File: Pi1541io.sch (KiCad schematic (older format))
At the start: 50 parts, among them J1 IEC1, J10 SDA, J11 SCL, J12 I2C, J2 IEC2, J3 IEC3, J4 ExtSpkr, J5 GS3, J6 GS3, J7 GS3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

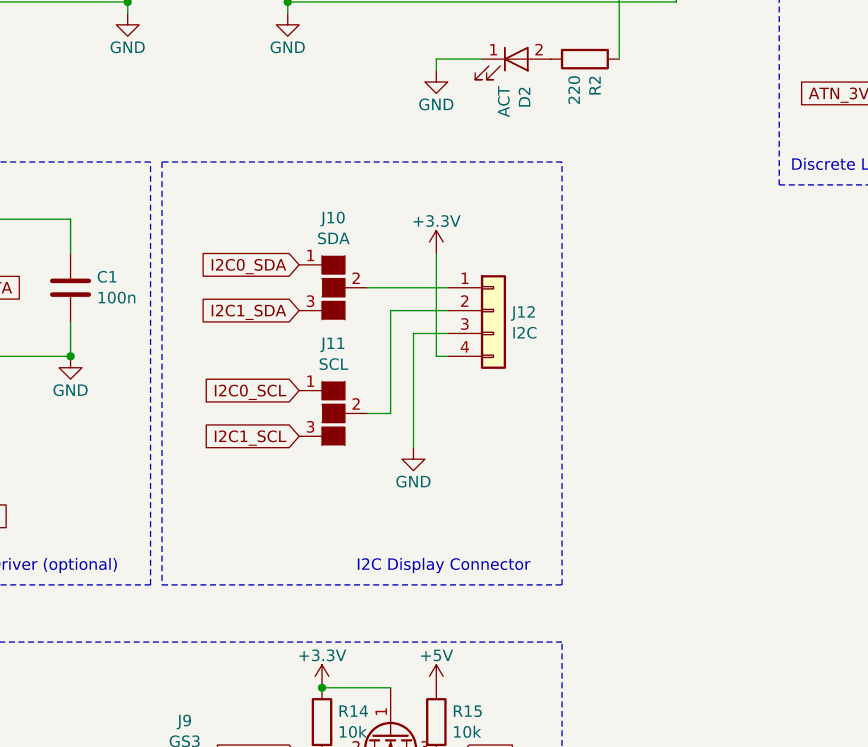
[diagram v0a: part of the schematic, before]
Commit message: I2C power pins now configurable.
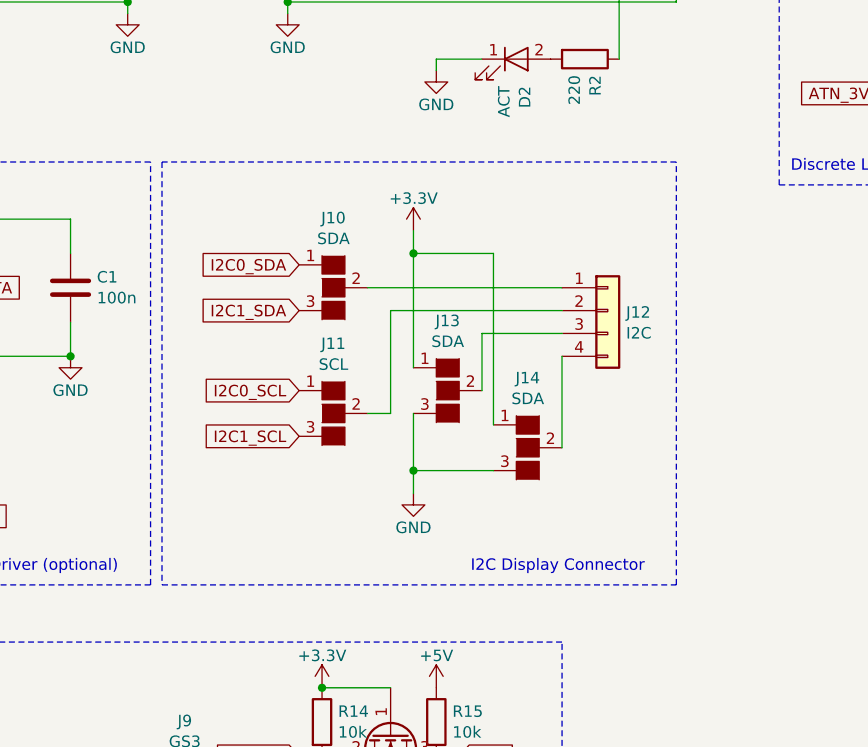
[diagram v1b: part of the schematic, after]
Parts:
- added J13, J14: SDA, Connectors:GS3, symbol conn:GS3
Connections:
- net +3V3: now also J13.1 (G1), J14.1 (G1); no longer J12.4 (Pin_4)
- net GND: now also J13.3 (G3), J14.3 (G3); no longer J12.3 (Pin_3)
- new net: J12.3 (Pin_3), J13.2 (G2)
- new net: J12.4 (Pin_4), J14.2 (G2)
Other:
- moved on the sheet: J12
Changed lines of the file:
@@
 L Pi1541io:Conn_01x04-Connector J12
 U 1 1 5B16BA02
-P 5000 4500
-F 0 "J12" H 5080 4492 50  0000 L CNN
-F 1 "I2C" H 5080 4401 50  0000 L CNN
-F 2 "Socket_Strips:Socket_Strip_Straight_1x04_Pitch2.54mm" H 5000 4500 50  0001 C CNN
-F 3 "~" H 5000 4500 50  0001 C CNN
-	1    5000 4500
+P 5500 4500
+F 0 "J12" H 5580 4492 50  0000 L CNN
+F 1 "I2C" H 5580 4401 50  0000 L CNN
+F 2 "Socket_Strips:Socket_Strip_Straight_1x04_Pitch2.54mm" H 5500 4500 50  0001 C CNN
+F 3 "~" H 5500 4500 50  0001 C CNN
+	1    5500 4500
 	1    0    0    -1
 $EndComp
@@
 $EndComp
 Wire Wire Line
-	4800 4400 4450 4400
-Wire Wire Line
-	4800 4600 4650 4600
-Wire Wire Line
-	4650 4600 4650 5100
-Wire Wire Line
-	4800 4700 4750 4700
-Wire Wire Line
-	4750 4700 4750 4250
+	5300 4400 4450 4400
 $Comp
 L power:GND #PWR0125
 U 1 1 5B1E56FA
-P 4650 5100
-F 0 "#PWR0125" H 4650 4850 50  0001 C CNN
-F 1 "GND" H 4650 4950 50  0000 C CNN
-F 2 "" H 4650 5100 50  0000 C CNN
-F 3 "" H 4650 5100 50  0000 C CNN
-	1    4650 5100
+P 4650 5300
+F 0 "#PWR0125" H 4650 5050 50  0001 C CNN
+F 1 "GND" H 4650 5150 50  0000 C CNN
+F 2 "" H 4650 5300 50  0000 C CNN
+F 3 "" H 4650 5300 50  0000 C CNN
+	1    4650 5300
 	1    0    0    -1
 $EndComp
 Wire Wire Line
-	4800 4500 4550 4500
+	5300 4500 4550 4500
 Wire Wire Line
 	4550 4500 4550 4950
@@
 	3550 3850 3550 5700
 Wire Notes Line
-	3550 5700 5300 5700
+	3550 5700 5800 5700
 Wire Notes Line
-	5300 5700 5300 3850
+	5800 5700 5800 3850
 Wire Notes Line
-	5300 3850 3550 3850
-Text Notes 4400 5650 0    50   ~ 0
+	5800 3850 3550 3850
+Text Notes 4900 5650 0    50   ~ 0
 I2C Display Connector
 $Comp
-L power:+3.3V #PWR?
+L power:+3.3V #PWR0124
 U 1 1 5B3C1A0C
-P 4750 4250
-F 0 "#PWR?" H 4750 4100 50  0001 C CNN
-F 1 "+3.3V" H 4750 4390 50  0000 C CNN
-F 2 "" H 4750 4250 50  0000 C CNN
-F 3 "" H 4750 4250 50  0000 C CNN
-	1    4750 4250
+P 4650 4150
+F 0 "#PWR0124" H 4650 4000 50  0001 C CNN
+F 1 "+3.3V" H 4650 4290 50  0000 C CNN
+F 2 "" H 4650 4150 50  0000 C CNN
+F 3 "" H 4650 4150 50  0000 C CNN
+	1    4650 4150
 	1    0    0    -1
 $EndComp
+$Comp
+L conn:GS3 J13
+U 1 1 5B409F64
+P 4800 4850
+F 0 "J13" H 4800 5155 50  0000 C CNN
+F 1 "SDA" H 4800 5064 50  0000 C CNN
+F 2 "Connectors:GS3" V 4888 4776 50  0001 C CNN
+F 3 "" H 4800 4850 50  0001 C CNN
+	1    4800 4850
+	1    0    0    -1
+$EndComp
+$Comp
+L conn:GS3 J14
+U 1 1 5B413348
+P 5150 5100
+F 0 "J14" H 5150 5405 50  0000 C CNN
+F 1 "SDA" H 5150 5314 50  0000 C CNN
+F 2 "Connectors:GS3" V 5238 5026 50  0001 C CNN
+F 3 "" H 5150 5100 50  0001 C CNN
+	1    5150 5100
+	1    0    0    -1
+$EndComp
+Wire Wire Line
+	5300 5100 5300 4700
+Wire Wire Line
+	5300 4600 4950 4600
+Wire Wire Line
+	4950 4600 4950 4850
+Wire Wire Line
+	4650 4950 4650 5200
+Wire Wire Line
+	5000 5200 4650 5200
+Connection ~ 4650 5200
+Wire Wire Line
+	4650 5200 4650 5300
+Wire Wire Line
+	4650 4750 4650 4250
+Wire Wire Line
+	5000 5000 5000 4250
+Wire Wire Line
+	5000 4250 4650 4250
+Connection ~ 4650 4250
+Wire Wire Line
+	4650 4250 4650 4150
 $EndSCHEMATC

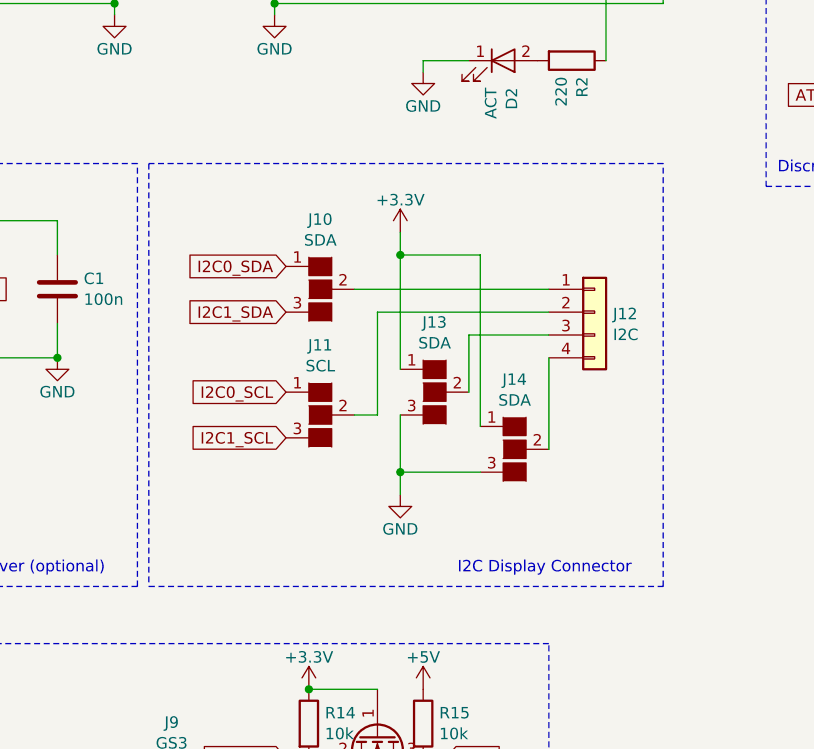
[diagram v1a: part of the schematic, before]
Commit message: Both voltage and pin order now configurable.
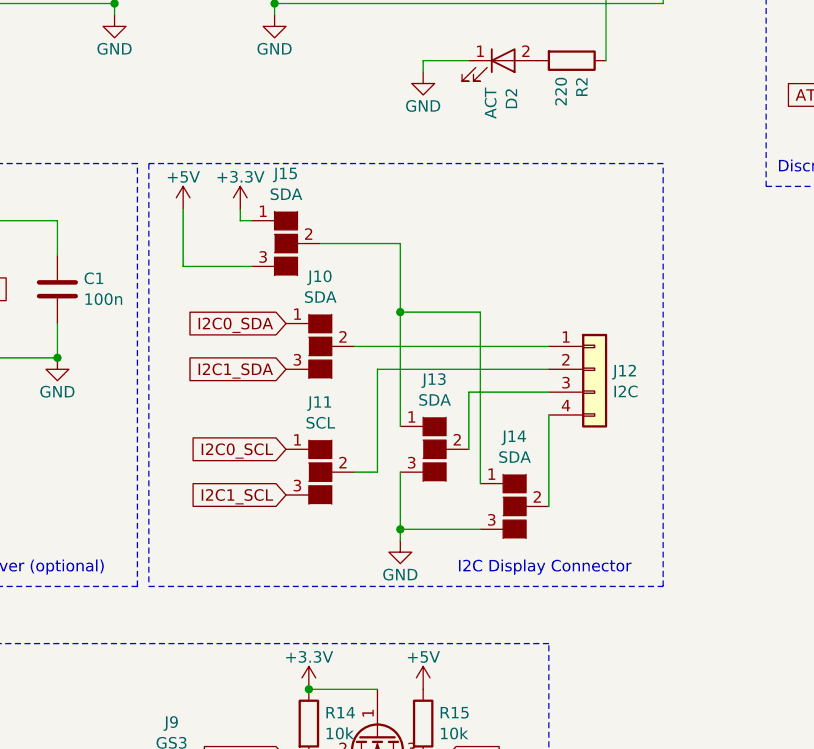
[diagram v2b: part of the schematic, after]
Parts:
- added J15: SDA, Connectors:GS3, symbol conn:GS3
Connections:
- net +3V3: now also J15.1 (G1); no longer J13.1 (G1), J14.1 (G1)
- net +5V: now also J15.3 (G3)
- new net: J13.1 (G1), J14.1 (G1), J15.2 (G2)
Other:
- moved on the sheet: J10, J11, J12, J13, J14
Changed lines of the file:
@@
 Sheet 1 1
 Title "Pi1541 IO Adapter"
-Date "2018-07-05"
+Date "2018-07-08"
 Rev "4"
 Comp "hackup.net"
@@
 L Pi1541io:Conn_01x04-Connector J12
 U 1 1 5B16BA02
-P 5500 4500
-F 0 "J12" H 5580 4492 50  0000 L CNN
-F 1 "I2C" H 5580 4401 50  0000 L CNN
-F 2 "Socket_Strips:Socket_Strip_Straight_1x04_Pitch2.54mm" H 5500 4500 50  0001 C CNN
-F 3 "~" H 5500 4500 50  0001 C CNN
-	1    5500 4500
+P 5500 4750
+F 0 "J12" H 5580 4742 50  0000 L CNN
+F 1 "I2C" H 5580 4651 50  0000 L CNN
+F 2 "Socket_Strips:Socket_Strip_Straight_1x04_Pitch2.54mm" H 5500 4750 50  0001 C CNN
+F 3 "~" H 5500 4750 50  0001 C CNN
+	1    5500 4750
 	1    0    0    -1
 $EndComp
@@
 L conn:GS3 J10
 U 1 1 5B1BB247
-P 4300 4400
-F 0 "J10" H 4300 4705 50  0000 C CNN
-F 1 "SDA" H 4300 4614 50  0000 C CNN
-F 2 "Connectors:GS3" V 4388 4326 50  0001 C CNN
-F 3 "" H 4300 4400 50  0001 C CNN
-	1    4300 4400
+P 4300 4650
+F 0 "J10" H 4300 4955 50  0000 C CNN
+F 1 "SDA" H 4300 4864 50  0000 C CNN
+F 2 "Connectors:GS3" V 4388 4576 50  0001 C CNN
+F 3 "" H 4300 4650 50  0001 C CNN
+	1    4300 4650
 	1    0    0    -1
 $EndComp
@@
 L conn:GS3 J11
 U 1 1 5B1BB619
-P 4300 4950
-F 0 "J11" H 4300 5255 50  0000 C CNN
-F 1 "SCL" H 4300 5164 50  0000 C CNN
-F 2 "Connectors:GS3" V 4388 4876 50  0001 C CNN
-F 3 "" H 4300 4950 50  0001 C CNN
-	1    4300 4950
-	1    0    0    -1
-$EndComp
-Wire Wire Line
-	5300 4400 4450 4400
+P 4300 5200
+F 0 "J11" H 4300 5505 50  0000 C CNN
+F 1 "SCL" H 4300 5414 50  0000 C CNN
+F 2 "Connectors:GS3" V 4388 5126 50  0001 C CNN
+F 3 "" H 4300 5200 50  0001 C CNN
+	1    4300 5200
+	1    0    0    -1
+$EndComp
+Wire Wire Line
+	5300 4650 4450 4650
 $Comp
 L power:GND #PWR0125
 U 1 1 5B1E56FA
-P 4650 5300
-F 0 "#PWR0125" H 4650 5050 50  0001 C CNN
-F 1 "GND" H 4650 5150 50  0000 C CNN
-F 2 "" H 4650 5300 50  0000 C CNN
-F 3 "" H 4650 5300 50  0000 C CNN
-	1    4650 5300
-	1    0    0    -1
-$EndComp
-Wire Wire Line
-	5300 4500 4550 4500
-Wire Wire Line
-	4550 4500 4550 4950
-Wire Wire Line
-	4550 4950 4450 4950
-Text GLabel 4150 4300 0    50   Input ~ 0
+P 4650 5500
+F 0 "#PWR0125" H 4650 5250 50  0001 C CNN
+F 1 "GND" H 4650 5350 50  0000 C CNN
+F 2 "" H 4650 5500 50  0000 C CNN
+F 3 "" H 4650 5500 50  0000 C CNN
+	1    4650 5500
+	1    0    0    -1
+$EndComp
+Wire Wire Line
+	5300 4750 4550 4750
+Wire Wire Line
+	4550 4750 4550 5200
+Wire Wire Line
+	4550 5200 4450 5200
+Text GLabel 4150 4550 0    50   Input ~ 0
 I2C0_SDA
-Text GLabel 4150 4500 0    50   Input ~ 0
+Text GLabel 4150 4750 0    50   Input ~ 0
 I2C1_SDA
-Text GLabel 4150 4850 0    50   Input ~ 0
+Text GLabel 4150 5100 0    50   Input ~ 0
 I2C0_SCL
-Text GLabel 4150 5050 0    50   Input ~ 0
+Text GLabel 4150 5300 0    50   Input ~ 0
 I2C1_SCL
 Wire Wire Line
@@
 L power:+3.3V #PWR0124
 U 1 1 5B3C1A0C
-P 4650 4150
-F 0 "#PWR0124" H 4650 4000 50  0001 C CNN
-F 1 "+3.3V" H 4650 4290 50  0000 C CNN
-F 2 "" H 4650 4150 50  0000 C CNN
-F 3 "" H 4650 4150 50  0000 C CNN
-	1    4650 4150
+P 3950 4050
+F 0 "#PWR0124" H 3950 3900 50  0001 C CNN
+F 1 "+3.3V" H 3950 4190 50  0000 C CNN
+F 2 "" H 3950 4050 50  0000 C CNN
+F 3 "" H 3950 4050 50  0000 C CNN
+	1    3950 4050
 	1    0    0    -1
 $EndComp
@@
 L conn:GS3 J13
 U 1 1 5B409F64
-P 4800 4850
-F 0 "J13" H 4800 5155 50  0000 C CNN
-F 1 "SDA" H 4800 5064 50  0000 C CNN
-F 2 "Connectors:GS3" V 4888 4776 50  0001 C CNN
-F 3 "" H 4800 4850 50  0001 C CNN
-	1    4800 4850
+P 4800 5100
+F 0 "J13" H 4800 5405 50  0000 C CNN
+F 1 "SDA" H 4800 5314 50  0000 C CNN
+F 2 "Connectors:GS3" V 4888 5026 50  0001 C CNN
+F 3 "" H 4800 5100 50  0001 C CNN
+	1    4800 5100
 	1    0    0    -1
 $EndComp
@@
 L conn:GS3 J14
 U 1 1 5B413348
-P 5150 5100
-F 0 "J14" H 5150 5405 50  0000 C CNN
-F 1 "SDA" H 5150 5314 50  0000 C CNN
-F 2 "Connectors:GS3" V 5238 5026 50  0001 C CNN
-F 3 "" H 5150 5100 50  0001 C CNN
-	1    5150 5100
-	1    0    0    -1
-$EndComp
-Wire Wire Line
-	5300 5100 5300 4700
-Wire Wire Line
-	5300 4600 4950 4600
-Wire Wire Line
-	4950 4600 4950 4850
-Wire Wire Line
-	4650 4950 4650 5200
-Wire Wire Line
-	5000 5200 4650 5200
-Connection ~ 4650 5200
-Wire Wire Line
-	4650 5200 4650 5300
-Wire Wire Line
-	4650 4750 4650 4250
-Wire Wire Line
-	5000 5000 5000 4250
-Wire Wire Line
-	5000 4250 4650 4250
-Connection ~ 4650 4250
-Wire Wire Line
-	4650 4250 4650 4150
+P 5150 5350
+F 0 "J14" H 5150 5655 50  0000 C CNN
+F 1 "SDA" H 5150 5564 50  0000 C CNN
+F 2 "Connectors:GS3" V 5238 5276 50  0001 C CNN
+F 3 "" H 5150 5350 50  0001 C CNN
+	1    5150 5350
+	1    0    0    -1
+$EndComp
+Wire Wire Line
+	5300 5350 5300 4950
+Wire Wire Line
+	5300 4850 4950 4850
+Wire Wire Line
+	4950 4850 4950 5100
+Wire Wire Line
+	4650 5200 4650 5450
+Wire Wire Line
+	5000 5450 4650 5450
+Connection ~ 4650 5450
+Wire Wire Line
+	4650 5450 4650 5500
+Wire Wire Line
+	4650 5000 4650 4500
+Wire Wire Line
+	5000 5250 5000 4500
+Wire Wire Line
+	5000 4500 4650 4500
+Connection ~ 4650 4500
+$Comp
+L conn:GS3 J15
+U 1 1 5B44E5B6
+P 4150 4200
+F 0 "J15" H 4150 4505 50  0000 C CNN
+F 1 "SDA" H 4150 4414 50  0000 C CNN
+F 2 "Connectors:GS3" V 4238 4126 50  0001 C CNN
+F 3 "" H 4150 4200 50  0001 C CNN
+	1    4150 4200
+	1    0    0    -1
+$EndComp
+$Comp
+L power:+5V #PWR0126
+U 1 1 5B44E7CA
+P 3700 4050
+F 0 "#PWR0126" H 3700 3900 50  0001 C CNN
+F 1 "+5V" H 3700 4190 50  0000 C CNN
+F 2 "" H 3700 4050 50  0000 C CNN
+F 3 "" H 3700 4050 50  0000 C CNN
+	1    3700 4050
+	1    0    0    -1
+$EndComp
+Wire Wire Line
+	3950 4050 3950 4100
+Wire Wire Line
+	3950 4100 4000 4100
+Wire Wire Line
+	4000 4300 3700 4300
+Wire Wire Line
+	3700 4300 3700 4050
+Wire Wire Line
+	4650 4200 4300 4200
+Wire Wire Line
+	4650 4200 4650 4500
 $EndSCHEMATC

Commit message: KiCAD 5.0.0.
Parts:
- MK1, MK2, MK3, MK4: symbol Mechanical:Mounting_Hole -> Mechanical:MountingHole
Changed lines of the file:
@@
 Connection ~ 4100 1750
 $Comp
-L Mechanical:Mounting_Hole MK1
+L Mechanical:MountingHole MK1
 U 1 1 5834FB2E
 P 750 7300
@@
 $EndComp
 $Comp
-L Mechanical:Mounting_Hole MK3
+L Mechanical:MountingHole MK3
 U 1 1 5834FBEF
 P 1200 7300
@@
 $EndComp
 $Comp
-L Mechanical:Mounting_Hole MK2
+L Mechanical:MountingHole MK2
 U 1 1 5834FC19
 P 750 7500
@@
 $EndComp
 $Comp
-L Mechanical:Mounting_Hole MK4
+L Mechanical:MountingHole MK4
 U 1 1 5834FC4F
 P 1200 7500

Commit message: Added additional drill holes for DIN connectors and polarity indicator for LEDs.
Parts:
- J1, J2: footprint DIN-Connector:DIN-6 -> DIN-Connector:DIN-6-Variable
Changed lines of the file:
@@
 Sheet 1 1
 Title "Pi1541 IO Adapter"
-Date "2018-07-08"
-Rev "4"
+Date "2018-09-04"
+Rev "4a"
 Comp "hackup.net"
 Comment1 "https://github.com/hackup/Pi1541io"
@@
 F 0 "J1" H 8800 4922 50  0000 C CNN
 F 1 "IEC1" H 8800 5013 50  0000 C CNN
-F 2 "DIN-Connector:DIN-6" H 8800 5400 50  0001 C CNN
+F 2 "DIN-Connector:DIN-6-Variable" H 8800 5400 50  0001 C CNN
 F 3 "http://www.mouser.com/ds/2/18/40_c091_abd_e-75918.pdf" H 8800 5400 50  0001 C CNN
 	1    8800 5400
@@
 F 0 "J2" H 9700 4922 50  0000 C CNN
 F 1 "IEC2" H 9700 5013 50  0000 C CNN
-F 2 "DIN-Connector:DIN-6" H 9700 5400 50  0001 C CNN
+F 2 "DIN-Connector:DIN-6-Variable" H 9700 5400 50  0001 C CNN
 F 3 "http://www.mouser.com/ds/2/18/40_c091_abd_e-75918.pdf" H 9700 5400 50  0001 C CNN
 	1    9700 5400

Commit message: Added ziptie holes.
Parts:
- added MK5, MK6: ZipTie, DIN-Connector:ZipTie_2.7mm, symbol Mechanical:MountingHole
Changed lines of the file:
@@
 Sheet 1 1
 Title "Pi1541 IO Adapter"
-Date "2018-09-04"
-Rev "4a"
+Date "2018-09-21"
+Rev "5"
 Comp "hackup.net"
 Comment1 "https://github.com/hackup/Pi1541io"
@@
 Wire Wire Line
 	4650 4200 4650 4500
+$Comp
+L Mechanical:MountingHole MK5
+U 1 1 5BA68CF3
+P 1800 7300
+F 0 "MK5" H 1900 7346 50  0000 L CNN
+F 1 "ZipTie" H 1900 7255 50  0000 L CNN
+F 2 "DIN-Connector:ZipTie_2.7mm" H 1800 7300 60  0001 C CNN
+F 3 "" H 1800 7300 60  0001 C CNN
+	1    1800 7300
+	1    0    0    -1
+$EndComp
+$Comp
+L Mechanical:MountingHole MK6
+U 1 1 5BA6979B
+P 1800 7500
+F 0 "MK6" H 1900 7546 50  0000 L CNN
+F 1 "ZipTie" H 1900 7455 50  0000 L CNN
+F 2 "DIN-Connector:ZipTie_2.7mm" H 1800 7500 60  0001 C CNN
+F 3 "" H 1800 7500 60  0001 C CNN
+	1    1800 7500
+	1    0    0    -1
+$EndComp
 $EndSCHEMATC

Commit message: Moved LEDs, texts, reset button, and speaker.
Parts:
- removed JP1: SPKR_EN, Pin_Headers:Pin_Header_Straight_1x02_Pitch2.54mm, symbol device:Jumper_NC_Small
- added SW7: SPKR_EN, Pin_Headers:Pin_Header_Straight_2x01_Pitch2.54mm, symbol Switch:SW_SPST
- J4: footprint Pin_Headers:Pin_Header_Straight_1x02_Pitch2.54mm -> Pin_Headers:Pin_Header_Straight_1x01_Pitch2.54mm; symbol conn:Conn_01x02 -> conn:Conn_01x01
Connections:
- wire segments 183 -> 179
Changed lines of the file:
@@
 U 1 1 5AF31714
 P 700 2750
-F 0 "LS1" H 667 2333 50  0000 C CNN
-F 1 "Spkr" H 667 2424 50  0000 C CNN
+F 0 "LS1" H 700 2400 50  0000 C CNN
+F 1 "Spkr" H 700 2500 50  0000 C CNN
 F 2 "hackup:Piezo Speaker 1407" H 665 2700 50  0001 C CNN
 F 3 "" H 665 2700 50  0001 C CNN
@@
 	-1   0    0    1
 $EndComp
-Wire Wire Line
-	900  2650 950  2650
 $Comp
 L device:LED D2
@@
 $EndComp
 $Comp
-L conn:Conn_01x02 J4
+L conn:Conn_01x01 J4
 U 1 1 5AF4251E
 P 700 3250
-F 0 "J4" H 620 2925 50  0000 C CNN
-F 1 "ExtSpkr" H 620 3016 50  0000 C CNN
-F 2 "Pin_Headers:Pin_Header_Straight_1x02_Pitch2.54mm" H 700 3250 50  0001 C CNN
+F 0 "J4" H 700 3350 50  0000 C CNN
+F 1 "ExtSpkr" H 700 3150 50  0000 C CNN
+F 2 "Pin_Headers:Pin_Header_Straight_1x01_Pitch2.54mm" H 700 3250 50  0001 C CNN
 F 3 "~" H 700 3250 50  0001 C CNN
 	1    700  3250
 	-1   0    0    1
 $EndComp
-Wire Wire Line
-	900  3150 950  3150
-Wire Wire Line
-	950  3150 950  2650
-Connection ~ 950  2650
 Wire Wire Line
 	900  3250 1050 3250
@@
 Wire Wire Line
 	1550 2650 1550 3150
-$Comp
-L device:Jumper_NC_Small JP1
-U 1 1 5B0F3F40
-P 1350 2750
-F 0 "JP1" H 1350 2700 50  0000 C CNN
-F 1 "SPKR_EN" H 1350 2850 50  0000 C CNN
-F 2 "Pin_Headers:Pin_Header_Straight_1x02_Pitch2.54mm" H 1350 2750 50  0001 C CNN
-F 3 "" H 1350 2750 50  0001 C CNN
-	1    1350 2750
-	-1   0    0    1
-$EndComp
-Wire Wire Line
-	1450 2750 3500 2750
-Wire Wire Line
-	1250 2750 1050 2750
 Wire Wire Line
 	1050 3250 1050 2750
-Connection ~ 1050 2750
 Wire Wire Line
 	1050 2750 900  2750
-Wire Wire Line
-	950  2650 1550 2650
 Wire Notes Line
 	5300 5950 950  5950
@@
 	1    0    0    -1
 $EndComp
+Wire Wire Line
+	900  2650 1550 2650
+$Comp
+L Switch:SW_SPST SW7
+U 1 1 5BB91903
+P 1250 2750
+F 0 "SW7" H 1250 2550 50  0000 C CNN
+F 1 "SPKR_EN" H 1250 2650 50  0000 C CNN
+F 2 "Pin_Headers:Pin_Header_Straight_2x01_Pitch2.54mm" H 1250 2750 50  0001 C CNN
+F 3 "" H 1250 2750 50  0001 C CNN
+	1    1250 2750
+	1    0    0    -1
+$EndComp
+Wire Wire Line
+	1450 2750 3500 2750
+Connection ~ 1050 2750
 $EndSCHEMATC

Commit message: Improved ziptie holes.
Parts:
- MK5, MK6: footprint DIN-Connector:ZipTie_2.7mm -> DIN-Connector:ZipTie_3.0mm
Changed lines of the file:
@@
 F 0 "MK5" H 1900 7346 50  0000 L CNN
 F 1 "ZipTie" H 1900 7255 50  0000 L CNN
-F 2 "DIN-Connector:ZipTie_2.7mm" H 1800 7300 60  0001 C CNN
+F 2 "DIN-Connector:ZipTie_3.0mm" H 1800 7300 60  0001 C CNN
 F 3 "" H 1800 7300 60  0001 C CNN
 	1    1800 7300
@@
 F 0 "MK6" H 1900 7546 50  0000 L CNN
 F 1 "ZipTie" H 1900 7455 50  0000 L CNN
-F 2 "DIN-Connector:ZipTie_2.7mm" H 1800 7500 60  0001 C CNN
+F 2 "DIN-Connector:ZipTie_3.0mm" H 1800 7500 60  0001 C CNN
 F 3 "" H 1800 7500 60  0001 C CNN
 	1    1800 7500
